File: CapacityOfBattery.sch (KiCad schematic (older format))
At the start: 17 parts, among them J1 BATTERY, J2 DUT, Q1 IRLML6401TRPBF, Q2 IRLML6401TRPBF, Q3 IRLML6401TRPBF, Q4 IRLML6401TRPBF, Q5 IRLML6401TRPBF, U1 NodeMCU1.0(ESP-12E)

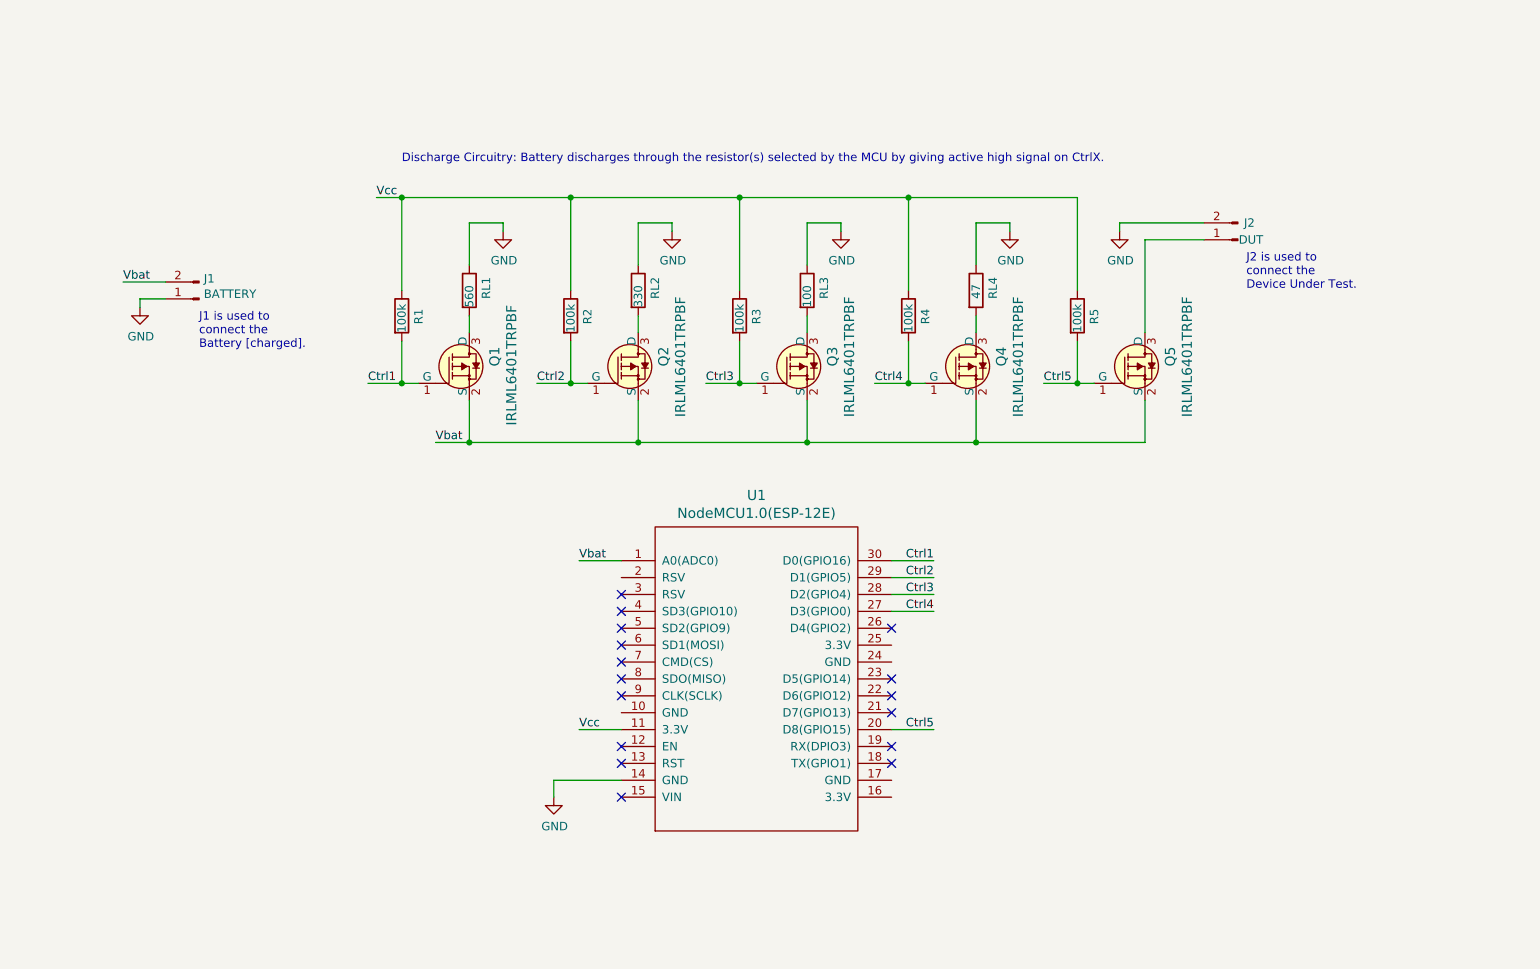
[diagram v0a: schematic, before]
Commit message: update schematic
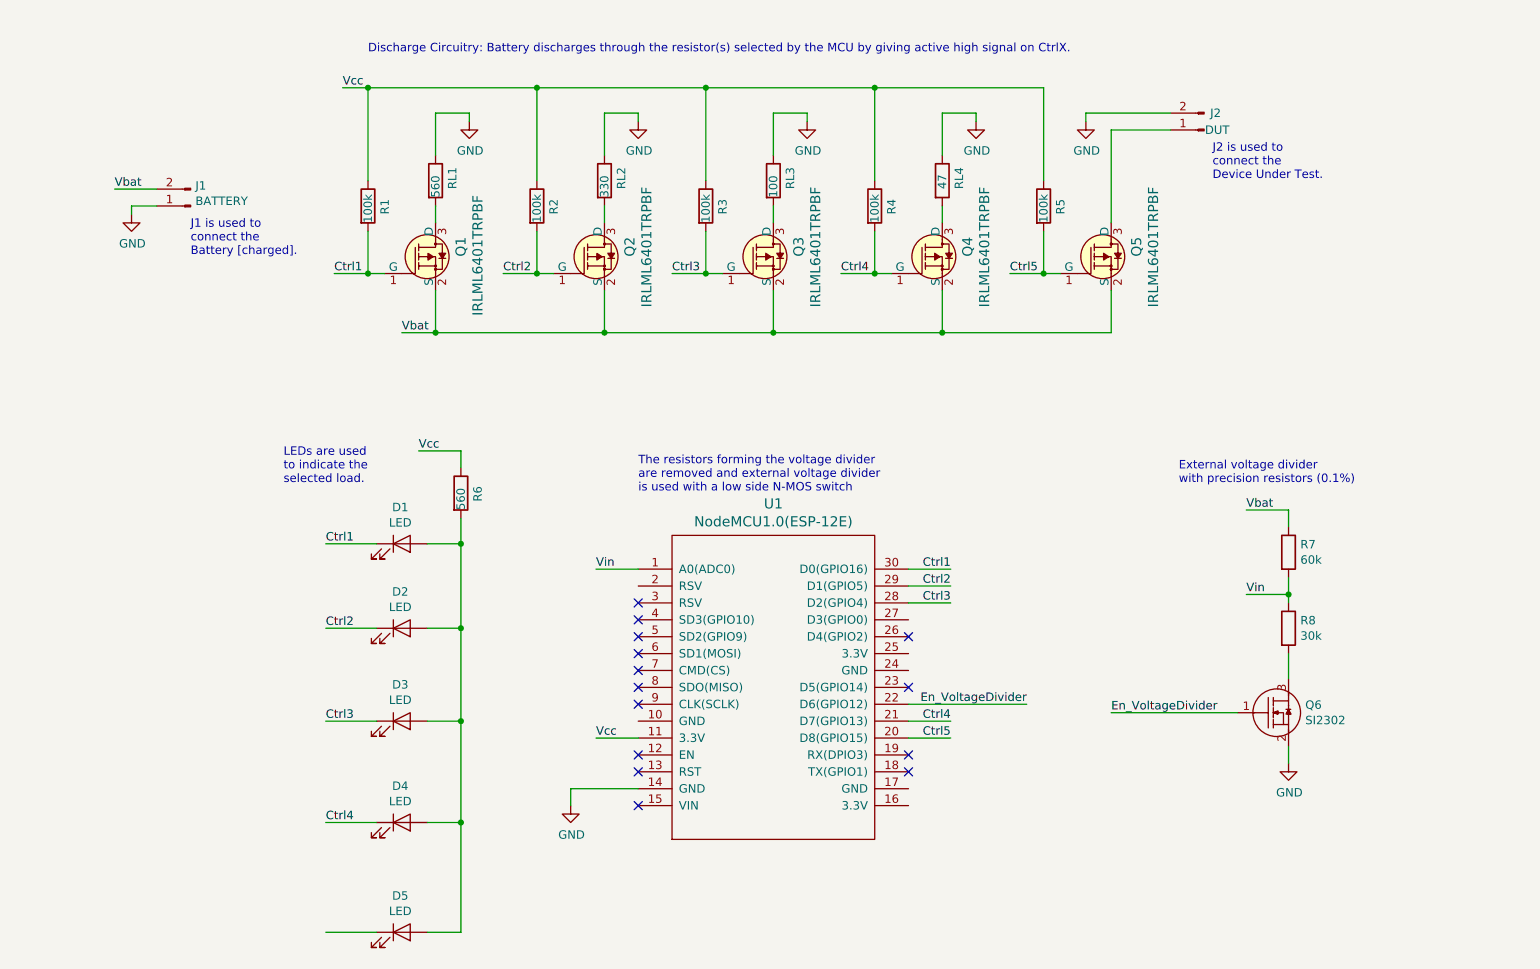
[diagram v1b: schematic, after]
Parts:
- added D1, D2, D3, D4, D5: LED, symbol Device:LED
- added Q6: SI2302, symbol Transistor_FET_SI2302:SI2302
- added R6: 560, symbol Device:R
- added R7: 60k, symbol Device:R
- added R8: 30k, symbol Device:R
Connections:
- net Ctrl1: now also D1.1 (K)
- net Ctrl2: now also D2.1 (K)
- net Ctrl3: now also D3.1 (K)
- net Ctrl4: now also U1.21 (D7(GPIO13)), D4.1 (K); no longer U1.27 (D3(GPIO0))
- net GND: now also Q6.2 (S)
- net Vbat: now also R7.1; no longer U1.1 (A0(ADC0))
- net Vcc: now also R6.1
- net En_VoltageDivider: now reaches U1.22 (D6(GPIO12))
- net En_VoltageDivider: now also Q6.1 (G)
- new net: D1.2 (A), D2.2 (A), D3.2 (A), D4.2 (A), D5.2 (A), R6.2
- new net: Q6.3 (D), R8.2
- new net Vin: R7.2, R8.1, U1.1 (A0(ADC0))
- no-connect marks 16 -> 14
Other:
- note added: "External voltage divider \nwith precision resistors (0.1%)"
- note added: "LEDs are used \nto indicate the \nselected load."
- note added: "The resistors forming the voltage divider \nare removed and external voltage divider \nis used with a low side N-MOS switch"
- moved on the sheet: J1, J2, Q1, Q2, Q3, Q4, Q5, R1, R2, R3, R4, R5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

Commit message: updated pcb
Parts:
- added R9: 10k, Resistor_SMD:R_0805_2012Metric_Pad1.15x1.40mm_HandSolder, symbol Device:R
- D1, D2, D3, D4, D5: footprint (none) -> LED_SMD:LED_0805_2012Metric_Pad1.15x1.40mm_HandSolder
- Q6: footprint (none) -> Package_TO_SOT_SMD:SOT-23
- R6, R7, R8: footprint (none) -> Resistor_SMD:R_0805_2012Metric_Pad1.15x1.40mm_HandSolder
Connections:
- net Ctrl5: now also D5.1 (K)
- net En_VoltageDivider: now also R9.2
- net GND: now also J2.1 (Pin_1), R9.1; no longer J2.2 (Pin_2)
- net at Q5.3 (D): now also J2.2 (Pin_2); no longer J2.1 (Pin_1)
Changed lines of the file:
@@
 L Connector:Conn_01x02_Male J2
 U 1 1 5CF76A7D
-P 8250 1800
-F 0 "J2" H 8150 1700 50  0000 L CNN
-F 1 "DUT" H 8100 1800 50  0000 L CNN
-F 2 "Connector_PinHeader_2.54mm:PinHeader_1x02_P2.54mm_Vertical" H 8250 1800 50  0001 C CNN
-F 3 "~" H 8250 1800 50  0001 C CNN
-	1    8250 1800
-	-1   0    0    1
+P 8250 1700
+F 0 "J2" H 8150 1600 50  0000 L CNN
+F 1 "DUT" H 8100 1700 50  0000 L CNN
+F 2 "Connector_PinHeader_2.54mm:PinHeader_1x02_P2.54mm_Vertical" H 8250 1700 50  0001 C CNN
+F 3 "~" H 8250 1700 50  0001 C CNN
+	1    8250 1700
+	-1   0    0    -1
 $EndComp
 $Comp
@@
 Text Notes 3300 1350 0    50   ~ 0
 Discharge Circuitry: Battery discharges through the resistor(s) selected by the MCU by giving active high signal on CtrlX.
-Text Notes 8300 2100 0    50   ~ 0
+Text Notes 8350 2100 0    50   ~ 0
 J2 is used to\nconnect the\nDevice Under Test.
 Text Notes 2250 2550 0    50   ~ 0
@@
 F 0 "D1" H 3491 4466 50  0000 C CNN
 F 1 "LED" H 3491 4375 50  0000 C CNN
-F 2 "" H 3500 4250 50  0001 C CNN
+F 2 "LED_SMD:LED_0805_2012Metric_Pad1.15x1.40mm_HandSolder" H 3500 4250 50  0001 C CNN
 F 3 "~" H 3500 4250 50  0001 C CNN
 	1    3500 4250
@@
 F 0 "D2" H 3491 4966 50  0000 C CNN
 F 1 "LED" H 3491 4875 50  0000 C CNN
-F 2 "" H 3500 4750 50  0001 C CNN
+F 2 "LED_SMD:LED_0805_2012Metric_Pad1.15x1.40mm_HandSolder" H 3500 4750 50  0001 C CNN
 F 3 "~" H 3500 4750 50  0001 C CNN
 	1    3500 4750
@@
 F 0 "D3" H 3491 5516 50  0000 C CNN
 F 1 "LED" H 3491 5425 50  0000 C CNN
-F 2 "" H 3500 5300 50  0001 C CNN
+F 2 "LED_SMD:LED_0805_2012Metric_Pad1.15x1.40mm_HandSolder" H 3500 5300 50  0001 C CNN
 F 3 "~" H 3500 5300 50  0001 C CNN
 	1    3500 5300
@@
 F 0 "D4" H 3491 6116 50  0000 C CNN
 F 1 "LED" H 3491 6025 50  0000 C CNN
-F 2 "" H 3500 5900 50  0001 C CNN
+F 2 "LED_SMD:LED_0805_2012Metric_Pad1.15x1.40mm_HandSolder" H 3500 5900 50  0001 C CNN
 F 3 "~" H 3500 5900 50  0001 C CNN
 	1    3500 5900
@@
 F 0 "D5" H 3491 6766 50  0000 C CNN
 F 1 "LED" H 3491 6675 50  0000 C CNN
-F 2 "" H 3500 6550 50  0001 C CNN
+F 2 "LED_SMD:LED_0805_2012Metric_Pad1.15x1.40mm_HandSolder" H 3500 6550 50  0001 C CNN
 F 3 "~" H 3500 6550 50  0001 C CNN
 	1    3500 6550
@@
 F 0 "R6" V 3950 3900 50  0000 L CNN
 F 1 "560" V 3850 3850 50  0000 L CNN
-F 2 "" V 3780 3950 50  0001 C CNN
+F 2 "Resistor_SMD:R_0805_2012Metric_Pad1.15x1.40mm_HandSolder" V 3780 3950 50  0001 C CNN
 F 3 "~" H 3850 3950 50  0001 C CNN
 	1    3850 3950
@@
 F 0 "R7" H 8820 4346 50  0000 L CNN
 F 1 "60k" H 8820 4255 50  0000 L CNN
-F 2 "" V 8680 4300 50  0001 C CNN
+F 2 "Resistor_SMD:R_0805_2012Metric_Pad1.15x1.40mm_HandSolder" V 8680 4300 50  0001 C CNN
 F 3 "~" H 8750 4300 50  0001 C CNN
 	1    8750 4300
@@
 F 0 "R8" H 8820 4796 50  0000 L CNN
 F 1 "30k" H 8820 4705 50  0000 L CNN
-F 2 "" V 8680 4750 50  0001 C CNN
+F 2 "Resistor_SMD:R_0805_2012Metric_Pad1.15x1.40mm_HandSolder" V 8680 4750 50  0001 C CNN
 F 3 "~" H 8750 4750 50  0001 C CNN
 	1    8750 4750
@@
 F 0 "Q6" H 8849 5296 50  0000 L CNN
 F 1 "SI2302" H 8849 5205 50  0000 L CNN
-F 2 "" H 8550 5550 50  0001 C CNN
+F 2 "Package_TO_SOT_SMD:SOT-23" H 8550 5550 50  0001 C CNN
 F 3 "" H 8550 5550 50  0001 C CNN
 	1    8750 5250
@@
 	8750 4900 8750 5050
 Wire Wire Line
-	8750 5450 8750 5550
+	8750 5450 8750 5500
 Wire Wire Line
 	8500 4050 8750 4050
@@
 En_VoltageDivider
 Wire Wire Line
-	7700 5250 8450 5250
+	7700 5250 8150 5250
 Wire Wire Line
 	8750 4550 8500 4550
@@
 Text Notes 8100 3900 0    50   ~ 0
 External voltage divider \nwith precision resistors (0.1%)
+$Comp
+L Device:R R9
+U 1 1 5D0F6D0C
+P 8300 5500
+F 0 "R9" V 8400 5500 50  0000 C CNN
+F 1 "10k" V 8300 5500 50  0000 C CNN
+F 2 "Resistor_SMD:R_0805_2012Metric_Pad1.15x1.40mm_HandSolder" V 8230 5500 50  0001 C CNN
+F 3 "~" H 8300 5500 50  0001 C CNN
+	1    8300 5500
+	0    1    1    0
+$EndComp
+Wire Wire Line
+	8450 5500 8750 5500
+Connection ~ 8750 5500
+Wire Wire Line
+	8750 5500 8750 5550
+Wire Wire Line
+	8150 5500 8150 5250
+Connection ~ 8150 5250
+Wire Wire Line
+	8150 5250 8450 5250
+Text Label 3050 6550 0    50   ~ 0
+Ctrl5
 $EndSCHEMATC

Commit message: updated pcb
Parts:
- RL2: value 330 -> 232
- RL3: value 100 -> 116
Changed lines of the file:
@@
 P 4700 2100
 F 0 "RL2" V 4800 2050 50  0000 L CNN
-F 1 "330" V 4700 2000 50  0000 L CNN
+F 1 "232" V 4700 2000 50  0000 L CNN
 F 2 "Resistor_SMD:R_0805_2012Metric_Pad1.15x1.40mm_HandSolder" V 4630 2100 50  0001 C CNN
 F 3 "~" H 4700 2100 50  0001 C CNN
@@
 P 5700 2100
 F 0 "RL3" V 5800 2050 50  0000 L CNN
-F 1 "100" V 5700 2000 50  0000 L CNN
+F 1 "116" V 5700 2000 50  0000 L CNN
 F 2 "Resistor_SMD:R_0805_2012Metric_Pad1.15x1.40mm_HandSolder" V 5630 2100 50  0001 C CNN
 F 3 "~" H 5700 2100 50  0001 C CNN

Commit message: modified PCB
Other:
- moved on the sheet: D1, D2, D3, D4, D5, R6
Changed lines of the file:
@@
 L Device:LED D1
 U 1 1 5D09C200
-P 3500 4250
-F 0 "D1" H 3491 4466 50  0000 C CNN
-F 1 "LED" H 3491 4375 50  0000 C CNN
-F 2 "LED_SMD:LED_0805_2012Metric_Pad1.15x1.40mm_HandSolder" H 3500 4250 50  0001 C CNN
-F 3 "~" H 3500 4250 50  0001 C CNN
-	1    3500 4250
+P 3250 4300
+F 0 "D1" H 3241 4516 50  0000 C CNN
+F 1 "LED" H 3241 4425 50  0000 C CNN
+F 2 "LED_SMD:LED_0805_2012Metric_Pad1.15x1.40mm_HandSolder" H 3250 4300 50  0001 C CNN
+F 3 "~" H 3250 4300 50  0001 C CNN
+	1    3250 4300
 	1    0    0    -1
 $EndComp
@@
 L Device:LED D2
 U 1 1 5D09C297
-P 3500 4750
-F 0 "D2" H 3491 4966 50  0000 C CNN
-F 1 "LED" H 3491 4875 50  0000 C CNN
-F 2 "LED_SMD:LED_0805_2012Metric_Pad1.15x1.40mm_HandSolder" H 3500 4750 50  0001 C CNN
-F 3 "~" H 3500 4750 50  0001 C CNN
-	1    3500 4750
+P 3250 4800
+F 0 "D2" H 3241 5016 50  0000 C CNN
+F 1 "LED" H 3241 4925 50  0000 C CNN
+F 2 "LED_SMD:LED_0805_2012Metric_Pad1.15x1.40mm_HandSolder" H 3250 4800 50  0001 C CNN
+F 3 "~" H 3250 4800 50  0001 C CNN
+	1    3250 4800
 	1    0    0    -1
 $EndComp
@@
 L Device:LED D3
 U 1 1 5D09D4AF
-P 3500 5300
-F 0 "D3" H 3491 5516 50  0000 C CNN
-F 1 "LED" H 3491 5425 50  0000 C CNN
-F 2 "LED_SMD:LED_0805_2012Metric_Pad1.15x1.40mm_HandSolder" H 3500 5300 50  0001 C CNN
-F 3 "~" H 3500 5300 50  0001 C CNN
-	1    3500 5300
+P 3250 5350
+F 0 "D3" H 3241 5566 50  0000 C CNN
+F 1 "LED" H 3241 5475 50  0000 C CNN
+F 2 "LED_SMD:LED_0805_2012Metric_Pad1.15x1.40mm_HandSolder" H 3250 5350 50  0001 C CNN
+F 3 "~" H 3250 5350 50  0001 C CNN
+	1    3250 5350
 	1    0    0    -1
 $EndComp
@@
 L Device:LED D4
 U 1 1 5D09E6D2
-P 3500 5900
-F 0 "D4" H 3491 6116 50  0000 C CNN
-F 1 "LED" H 3491 6025 50  0000 C CNN
-F 2 "LED_SMD:LED_0805_2012Metric_Pad1.15x1.40mm_HandSolder" H 3500 5900 50  0001 C CNN
-F 3 "~" H 3500 5900 50  0001 C CNN
-	1    3500 5900
+P 3250 5950
+F 0 "D4" H 3241 6166 50  0000 C CNN
+F 1 "LED" H 3241 6075 50  0000 C CNN
+F 2 "LED_SMD:LED_0805_2012Metric_Pad1.15x1.40mm_HandSolder" H 3250 5950 50  0001 C CNN
+F 3 "~" H 3250 5950 50  0001 C CNN
+	1    3250 5950
 	1    0    0    -1
 $EndComp
@@
 L Device:LED D5
 U 1 1 5D09F8E6
-P 3500 6550
-F 0 "D5" H 3491 6766 50  0000 C CNN
-F 1 "LED" H 3491 6675 50  0000 C CNN
-F 2 "LED_SMD:LED_0805_2012Metric_Pad1.15x1.40mm_HandSolder" H 3500 6550 50  0001 C CNN
-F 3 "~" H 3500 6550 50  0001 C CNN
-	1    3500 6550
-	1    0    0    -1
-$EndComp
-Wire Wire Line
-	3850 6550 3650 6550
-Wire Wire Line
-	3650 5900 3850 5900
-Wire Wire Line
-	3850 4250 3850 4750
-Connection ~ 3850 5900
-Wire Wire Line
-	3850 5900 3850 6550
-Wire Wire Line
-	3650 5300 3850 5300
-Connection ~ 3850 5300
-Wire Wire Line
-	3850 5300 3850 5900
-Wire Wire Line
-	3650 4750 3850 4750
-Connection ~ 3850 4750
-Wire Wire Line
-	3850 4750 3850 5300
-Wire Wire Line
-	3650 4250 3850 4250
+P 3250 6600
+F 0 "D5" H 3241 6816 50  0000 C CNN
+F 1 "LED" H 3241 6725 50  0000 C CNN
+F 2 "LED_SMD:LED_0805_2012Metric_Pad1.15x1.40mm_HandSolder" H 3250 6600 50  0001 C CNN
+F 3 "~" H 3250 6600 50  0001 C CNN
+	1    3250 6600
+	1    0    0    -1
+$EndComp
+Wire Wire Line
+	3600 6600 3400 6600
+Wire Wire Line
+	3400 5950 3600 5950
+Wire Wire Line
+	3600 4300 3600 4800
+Connection ~ 3600 5950
+Wire Wire Line
+	3600 5950 3600 6600
+Wire Wire Line
+	3400 5350 3600 5350
+Connection ~ 3600 5350
+Wire Wire Line
+	3600 5350 3600 5950
+Wire Wire Line
+	3400 4800 3600 4800
+Connection ~ 3600 4800
+Wire Wire Line
+	3600 4800 3600 5350
+Wire Wire Line
+	3400 4300 3600 4300
 $Comp
 L Device:R R6
 U 1 1 5D0A7E09
-P 3850 3950
-F 0 "R6" V 3950 3900 50  0000 L CNN
-F 1 "560" V 3850 3850 50  0000 L CNN
-F 2 "Resistor_SMD:R_0805_2012Metric_Pad1.15x1.40mm_HandSolder" V 3780 3950 50  0001 C CNN
-F 3 "~" H 3850 3950 50  0001 C CNN
-	1    3850 3950
-	1    0    0    -1
-$EndComp
-Wire Wire Line
-	3850 4100 3850 4250
-Connection ~ 3850 4250
-Wire Wire Line
-	3850 3800 3850 3700
-Wire Wire Line
-	3850 3700 3600 3700
-Wire Wire Line
-	3050 4250 3350 4250
-Wire Wire Line
-	3050 4750 3350 4750
-Wire Wire Line
-	3050 5300 3350 5300
-Wire Wire Line
-	3050 5900 3350 5900
-Wire Wire Line
-	3050 6550 3350 6550
-Text Label 3600 3700 0    50   ~ 0
+P 3600 4000
+F 0 "R6" V 3700 3950 50  0000 L CNN
+F 1 "560" V 3600 3900 50  0000 L CNN
+F 2 "Resistor_SMD:R_0805_2012Metric_Pad1.15x1.40mm_HandSolder" V 3530 4000 50  0001 C CNN
+F 3 "~" H 3600 4000 50  0001 C CNN
+	1    3600 4000
+	1    0    0    -1
+$EndComp
+Wire Wire Line
+	3600 4150 3600 4300
+Connection ~ 3600 4300
+Wire Wire Line
+	3600 3850 3600 3750
+Wire Wire Line
+	3600 3750 3350 3750
+Wire Wire Line
+	2800 4300 3100 4300
+Wire Wire Line
+	2800 4800 3100 4800
+Wire Wire Line
+	2800 5350 3100 5350
+Wire Wire Line
+	2800 5950 3100 5950
+Wire Wire Line
+	2800 6600 3100 6600
+Text Label 3350 3750 0    50   ~ 0
 Vcc
-Text Label 3050 4250 0    50   ~ 0
+Text Label 2800 4300 0    50   ~ 0
 Ctrl1
-Text Label 3050 4750 0    50   ~ 0
+Text Label 2800 4800 0    50   ~ 0
 Ctrl2
-Text Label 3050 5300 0    50   ~ 0
+Text Label 2800 5350 0    50   ~ 0
 Ctrl3
-Text Label 3050 5900 0    50   ~ 0
+Text Label 2800 5950 0    50   ~ 0
 Ctrl4
-Text Notes 2800 3900 0    50   ~ 0
+Text Notes 2550 3950 0    50   ~ 0
 LEDs are used \nto indicate the \nselected load.
 Text Label 7200 5200 2    50   ~ 0
@@
 Wire Wire Line
 	8150 5250 8450 5250
-Text Label 3050 6550 0    50   ~ 0
+Text Label 2800 6600 0    50   ~ 0
 Ctrl5
 $EndSCHEMATC

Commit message: modified pcb
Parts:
- removed D5: LED, LED_SMD:LED_0805_2012Metric_Pad1.15x1.40mm_HandSolder, symbol Device:LED
- removed Q4: IRLML6401TRPBF, Package_TO_SOT_SMD:SOT-23, symbol dk_Transistors-FETs-MOSFETs-Single:IRLML6401TRPBF
- removed R4: 100k, Resistor_SMD:R_0805_2012Metric_Pad1.15x1.40mm_HandSolder, symbol Device:R
- removed RL4: 47, Resistor_SMD:R_0805_2012Metric_Pad1.15x1.40mm_HandSolder, symbol Device:R
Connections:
- net labels added: En_VD, LED1, LED2, LED3, LED4, SW, dut
- net labels removed: En_VoltageDivider
- wire segments 97 -> 79
- no-connect marks 14 -> 10
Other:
- moved on the sheet: J1, J2, Q1, Q2, Q3, Q5, R1, R2, R3, R5, RL1, RL2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

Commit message: update pcb
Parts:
- added R9: 1k, Resistor_SMD:R_0805_2012Metric_Pad1.15x1.40mm_HandSolder, symbol Device:R
- added SW1: SW_Push, Button_Switch_THT:SW_PUSH_6mm, symbol Switch:SW_Push
- renumbered Q5 to Q4, Q6 to Q5, R6 to R2, R2 to R3, R3 to R4, R9 to R6
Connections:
- net labels removed: Ctrl5
- wire segments 79 -> 83
- no-connect marks 10 -> 11
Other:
- note added: "A switch is used \nto select the load\n(Active HIGH)"
- moved on the sheet: J1, J2, Q1, Q2, Q3, Q4, R1, R3, R4, R5, RL1, RL2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

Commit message: changed pcb layout
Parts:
- added RL? (x2): 232, Resistor_SMD:R_0805_2012Metric_Pad1.15x1.40mm_HandSolder, symbol Device:R
- RL1: value 560 -> 232
- RL3: value 116 -> 232
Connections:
- net GND: now also RL?.2, RL?.2; no longer RL1.2
- net at Q3.3 (D), RL3.1: now also RL?.1
- new net: RL1.2, RL?.1
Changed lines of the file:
@@
 P 2900 2750
 F 0 "RL1" V 3000 2700 50  0000 L CNN
-F 1 "560" V 2900 2650 50  0000 L CNN
+F 1 "232" V 2900 2650 50  0000 L CNN
 F 2 "Resistor_SMD:R_0805_2012Metric_Pad1.15x1.40mm_HandSolder" V 2830 2750 50  0001 C CNN
 F 3 "~" H 2900 2750 50  0001 C CNN
@@
 P 5600 2800
 F 0 "RL3" V 5700 2750 50  0000 L CNN
-F 1 "116" V 5600 2700 50  0000 L CNN
+F 1 "232" V 5600 2700 50  0000 L CNN
 F 2 "Resistor_SMD:R_0805_2012Metric_Pad1.15x1.40mm_HandSolder" V 5530 2800 50  0001 C CNN
 F 3 "~" H 5600 2800 50  0001 C CNN
@@
 $EndComp
 Wire Wire Line
-	2900 2900 2900 3000
+	2900 3250 2900 3350
 Wire Wire Line
 	4250 2950 4250 3050
 Wire Wire Line
-	5600 2950 5600 3050
+	5600 2950 5600 3000
 Wire Wire Line
 	2500 1950 2500 2200
@@
 	4250 2550 4250 2650
 Wire Wire Line
-	5600 2550 5600 2650
+	5600 2550 5600 2600
 Wire Wire Line
 	2500 1450 2500 1650
@@
 L power:GND #PWR01
 U 1 1 5D0FB55F
-P 2900 3000
-F 0 "#PWR01" H 2900 2750 50  0001 C CNN
-F 1 "GND" H 2905 2827 50  0000 C CNN
-F 2 "" H 2900 3000 50  0001 C CNN
-F 3 "" H 2900 3000 50  0001 C CNN
-	1    2900 3000
+P 2900 3350
+F 0 "#PWR01" H 2900 3100 50  0001 C CNN
+F 1 "GND" H 2905 3177 50  0000 C CNN
+F 2 "" H 2900 3350 50  0001 C CNN
+F 3 "" H 2900 3350 50  0001 C CNN
+	1    2900 3350
 	1    0    0    -1
 $EndComp
@@
 Text Notes 9050 2850 0    50   ~ 0
 A switch is used \nto select the load\n(Active HIGH)
+$Comp
+L Device:R RL?
+U 1 1 5D0C89B4
+P 2900 3100
+F 0 "RL?" V 3000 3050 50  0000 L CNN
+F 1 "232" V 2900 3000 50  0000 L CNN
+F 2 "Resistor_SMD:R_0805_2012Metric_Pad1.15x1.40mm_HandSolder" V 2830 3100 50  0001 C CNN
+F 3 "~" H 2900 3100 50  0001 C CNN
+	1    2900 3100
+	1    0    0    -1
+$EndComp
+Wire Wire Line
+	2900 2950 2900 2900
+$Comp
+L Device:R RL?
+U 1 1 5D0CC57E
+P 5350 2800
+F 0 "RL?" V 5450 2750 50  0000 L CNN
+F 1 "232" V 5350 2700 50  0000 L CNN
+F 2 "Resistor_SMD:R_0805_2012Metric_Pad1.15x1.40mm_HandSolder" V 5280 2800 50  0001 C CNN
+F 3 "~" H 5350 2800 50  0001 C CNN
+	1    5350 2800
+	1    0    0    -1
+$EndComp
+Wire Wire Line
+	5350 2650 5350 2600
+Wire Wire Line
+	5350 2600 5600 2600
+Connection ~ 5600 2600
+Wire Wire Line
+	5600 2600 5600 2650
+Wire Wire Line
+	5350 2950 5350 3000
+Wire Wire Line
+	5350 3000 5600 3000
+Connection ~ 5600 3000
+Wire Wire Line
+	5600 3000 5600 3050
 $EndSCHEMATC
